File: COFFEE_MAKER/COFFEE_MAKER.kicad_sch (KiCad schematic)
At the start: 54 parts, among them J1 Conn_01x04, J2 Conn_01x06, J3 Conn_01x02_Pin, J4 Screw_Terminal_01x02, J5 USB_C_Receptacle_USB2.0_16P, J6 Conn_01x02_Pin, Q1 BC850, SW5 Reset, SW6 Boot, U3 AMS1117-3.3, U4 PCF8574, U5 MAX31855KASA, U6 AMS1117-5.0, U7 LD1117S33TR_SOT223, U8 ESP32-S2-SOLO

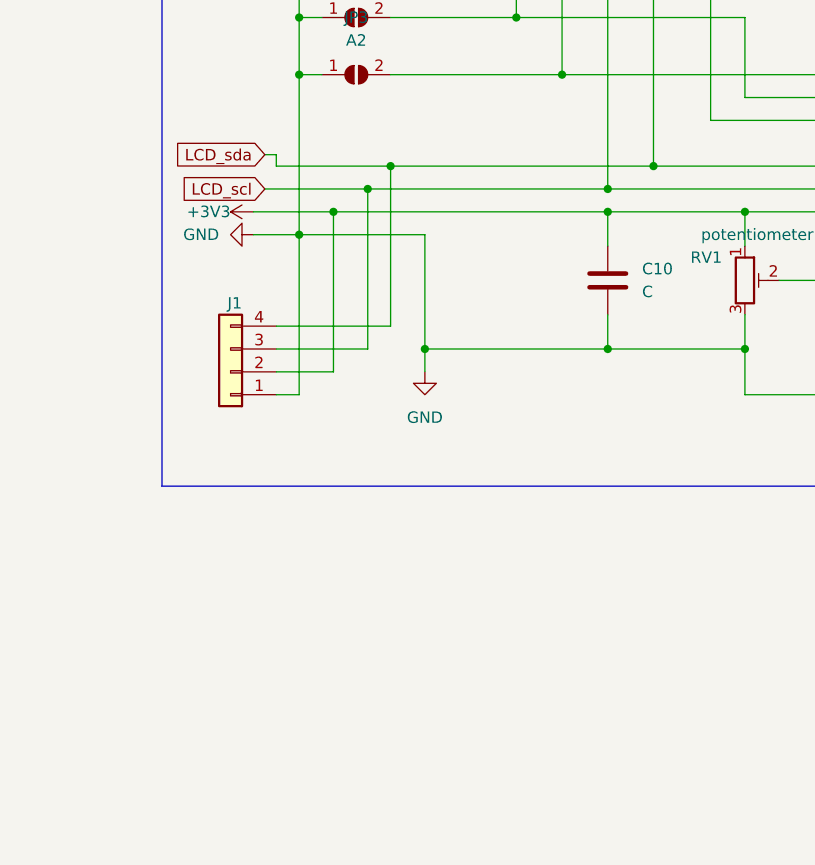
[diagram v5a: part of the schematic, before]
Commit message: added backup i2c pin, change lcd voltage to 5v
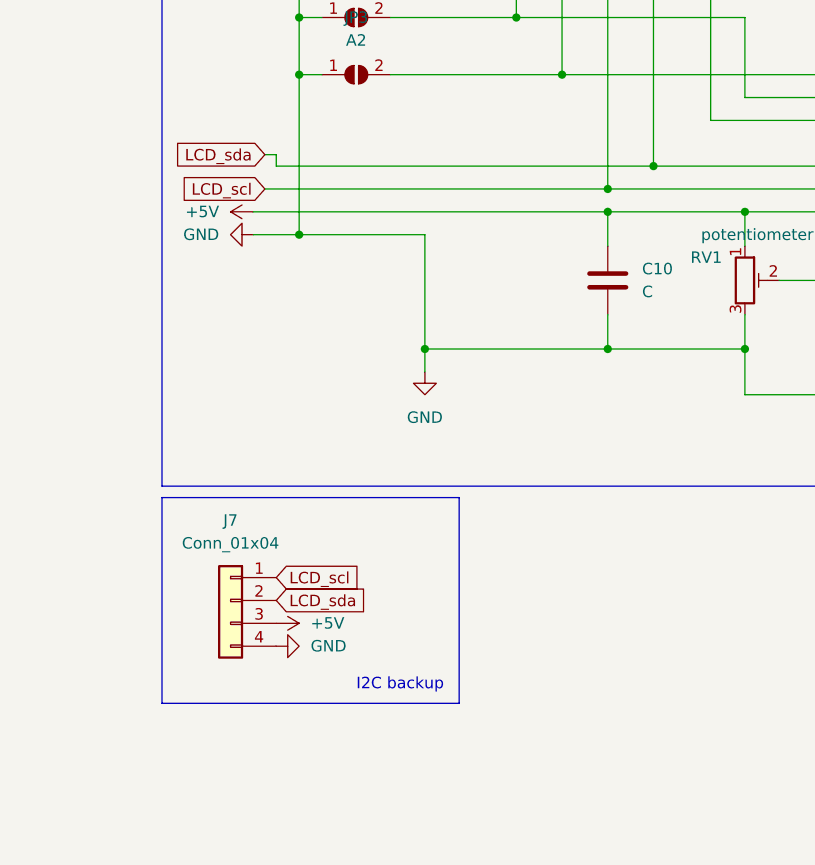
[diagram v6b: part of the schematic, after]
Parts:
- removed J1: Conn_01x04, symbol Connector_Generic:Conn_01x04
- added J7: Conn_01x04, symbol Connector_Generic:Conn_01x04
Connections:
- net +3V3: no longer C10.1, C16.1, C4.2, DS1.4 (VDD), F2.2, J5.A4 (VBUS), J5.A9 (VBUS), J5.B4 (VBUS), J5.B9 (VBUS), JP4.2 (B), R11.1, R12.1, R13.2, R14.1, R5.1, R6.1, R7.1, RV1.1, U4.8 (VSS), U7.3 (VI)
- net GND: now also J7.4 (Pin_4)
- net LCD_scl: now also J7.1 (Pin_1)
- net LCD_sda: now also J7.2 (Pin_2)
- new net +5V: C10.1, C16.1, C4.2, DS1.4 (VDD), F2.2, J5.A4 (VBUS), J5.A9 (VBUS), J5.B4 (VBUS), J5.B9 (VBUS), J7.3 (Pin_3), JP4.2 (B), R11.1, R12.1, R13.2, R14.1, R5.1, R6.1, R7.1, RV1.1, U4.8 (VSS), U7.3 (VI)
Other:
- note added: "I2C backup"
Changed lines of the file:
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@@
   (junction (at 207.01 124.46) (diameter 0) (color 0 0 0 0)
   )
-  (junction (at 38.1 57.15) (diameter 0) (color 0 0 0 0)
-  )
   (junction (at -229.87 106.68) (diameter 0) (color 0 0 0 0)
   )
@@
   (junction (at -29.21 60.96) (diameter 0) (color 0 0 0 0)
   )
-  (junction (at 35.56 59.69) (diameter 0) (color 0 0 0 0)
-  )
   (junction (at -165.1 35.56) (diameter 0) (color 0 0 0 0)
   )
@@
   )
   (junction (at 255.27 130.81) (diameter 0) (color 0 0 0 0)
-  )
-  (junction (at 31.75 62.23) (diameter 0) (color 0 0 0 0)
   )
   (junction (at -161.29 35.56) (diameter 0) (color 0 0 0 0)
@@
   (no_connect (at -58.42 60.96))
   (no_connect (at -149.86 58.42))
-  (wire (pts (xy 25.4 80.01) (xy 31.75 80.01))
-    (stroke (width 0) (type default))
-  )
   (wire (pts (xy 217.17 128.27) (xy 217.17 124.46))
     (stroke (width 0) (type default))
   )
-  (wire (pts (xy 35.56 59.69) (xy 62.23 59.69))
-    (stroke (width 0) (type default))
-  )
   (wire (pts (xy 77.47 62.23) (xy 90.17 62.23))
     (stroke (width 0) (type default))
@@
     (stroke (width 0) (type default))
   )
-  (wire (pts (xy 38.1 57.15) (xy 67.31 57.15))
-    (stroke (width 0) (type default))
-  )
   (wire (pts (xy -204.47 31.75) (xy -204.47 33.02))
     (stroke (width 0) (type default))
@@
     (stroke (width 0) (type default))
   )
-  (wire (pts (xy 25.4 77.47) (xy 35.56 77.47))
-    (stroke (width 0) (type default))
-  )
   (wire (pts (xy 165.1 69.85) (xy 132.08 69.85))
     (stroke (width 0) (type default))
@@
     (stroke (width 0) (type default))
   )
-  (wire (pts (xy 25.4 82.55) (xy 27.94 82.55))
-    (stroke (width 0) (type default))
-  )
   (wire (pts (xy 140.97 41.91) (xy 140.97 57.15))
     (stroke (width 0) (type default))
@@
     (stroke (width 0) (type default))
   )
-  (wire (pts (xy 27.94 82.55) (xy 27.94 64.77))
-    (stroke (width 0) (type default))
-  )
   (wire (pts (xy 137.16 77.47) (xy 119.38 77.47))
     (stroke (width 0) (type default))
@@
     (stroke (width 0) (type default))
   )
-  (wire (pts (xy 31.75 62.23) (xy 62.23 62.23))
-    (stroke (width 0) (type default))
-  )
   (wire (pts (xy -161.29 35.56) (xy -149.86 35.56))
     (stroke (width 0) (type default))
@@
     (stroke (width 0) (type default))
   )
-  (wire (pts (xy 24.13 59.69) (xy 35.56 59.69))
+  (wire (pts (xy 24.13 59.69) (xy 62.23 59.69))
     (stroke (width 0) (type default))
   )
@@
     (stroke (width 0) (type default))
   )
-  (wire (pts (xy 25.4 74.93) (xy 38.1 74.93))
-    (stroke (width 0) (type default))
-  )
   (wire (pts (xy 90.17 21.59) (xy 77.47 21.59))
     (stroke (width 0) (type default))
@@
     (stroke (width 0) (type default))
   )
-  (wire (pts (xy 22.86 62.23) (xy 31.75 62.23))
+  (wire (pts (xy 22.86 62.23) (xy 62.23 62.23))
     (stroke (width 0) (type default))
   )
@@
     (stroke (width 0) (type default))
   )
-  (wire (pts (xy 38.1 74.93) (xy 38.1 57.15))
-    (stroke (width 0) (type default))
-  )
   (wire (pts (xy 252.73 125.73) (xy 261.62 125.73))
     (stroke (width 0) (type default))
@@
     (stroke (width 0) (type default))
   )
-  (wire (pts (xy 35.56 77.47) (xy 35.56 59.69))
-    (stroke (width 0) (type default))
-  )
   (wire (pts (xy 241.3 130.81) (xy 245.11 130.81))
     (stroke (width 0) (type default))
@@
     (stroke (width 0) (type default))
   )
-  (wire (pts (xy 31.75 80.01) (xy 31.75 62.23))
-    (stroke (width 0) (type default))
-  )
   (wire (pts (xy -58.42 50.8) (xy -39.37 50.8))
     (stroke (width 0) (type default))
@@
     (stroke (width 0) (type default))
   )
-  (wire (pts (xy 25.4 57.15) (xy 38.1 57.15))
+  (wire (pts (xy 25.4 57.15) (xy 67.31 57.15))
     (stroke (width 0) (type default))
   )
@@
     (fill (type none))
   )
+  (rectangle (start 45.72 116.84) (end 12.7 93.98)
+    (stroke (width 0) (type default))
+    (fill (type none))
+  )
   (rectangle (start 124.46 114.3) (end 153.67 146.05)
     (stroke (width 0) (type default))
@@
   )
   (text "LCD I2C" (at 158.75 91.44 0)
+    (effects (font (size 1.27 1.27)) (justify left bottom))
+  )
+  (text "I2C backup\n" (at 34.29 115.57 0)
     (effects (font (size 1.27 1.27)) (justify left bottom))
   )
@@
     )
   )
+  (global_label "LCD_sda" (shape input) (at 25.4 105.41 0) (fields_autoplaced)
+    (effects (font (size 1.27 1.27)) (justify left))
+    (property "Intersheetrefs" "${INTERSHEET_REFS}" (at 36.247 105.41 0)
+      (effects (font (size 1.27 1.27)) (justify left) hide)
+    )
+  )
   (global_label "TC_cs" (shape input) (at -48.26 88.9 0) (fields_autoplaced)
     (effects (font (size 1.27 1.27)) (justify left))
@@
     )
   )
+  (global_label "LCD_scl" (shape input) (at 25.4 102.87 0) (fields_autoplaced)
+    (effects (font (size 1.27 1.27)) (justify left))
+    (property "Intersheetrefs" "${INTERSHEET_REFS}" (at 35.7028 102.87 0)
+      (effects (font (size 1.27 1.27)) (justify left) hide)
+    )
+  )
   (global_label "LCD_scl" (shape input) (at -48.26 74.93 0) (fields_autoplaced)
     (effects (font (size 1.27 1.27)) (justify left))
@@
         (path "/d1855ae5-bac9-4f6d-b11e-fad99d05f143"
           (reference "RV1") (unit 1)
+        )
+      )
+    )
+  )
+  (symbol (lib_id "power:+5V") (at 25.4 107.95 270) (unit 1)
+    (in_bom yes) (on_board yes) (dnp no) (fields_autoplaced)
+    (property "Reference" "#PWR08" (at 21.59 107.95 0)
+      (effects (font (size 1.27 1.27)) hide)
+    )
+    (property "Value" "+5V" (at 29.21 107.95 90)
+      (effects (font (size 1.27 1.27)) (justify left))
+    )
+    (property "Footprint" "" (at 25.4 107.95 0)
+      (effects (font (size 1.27 1.27)) hide)
+    )
+    (property "Datasheet" "" (at 25.4 107.95 0)
+      (effects (font (size 1.27 1.27)) hide)
+    )
+    (pin "1")
+    (instances
+      (project "COFFEE_MAKER"
+        (path "/d1855ae5-bac9-4f6d-b11e-fad99d05f143"
+          (reference "#PWR08") (unit 1)
         )
       )
@@
     )
   )
-  (symbol (lib_id "power:+3V3") (at 22.86 62.23 90) (unit 1)
-    (in_bom yes) (on_board yes) (dnp no)
-    (property "Reference" "#PWR02" (at 26.67 62.23 0)
-      (effects (font (size 1.27 1.27)) hide)
-    )
-    (property "Value" "+3V3" (at 20.32 62.23 90)
-      (effects (font (size 1.27 1.27)) (justify left))
-    )
-    (property "Footprint" "" (at 22.86 62.23 0)
-      (effects (font (size 1.27 1.27)) hide)
-    )
-    (property "Datasheet" "" (at 22.86 62.23 0)
-      (effects (font (size 1.27 1.27)) hide)
-    )
-    (pin "1")
-    (instances
-      (project "COFFEE_MAKER"
-        (path "/d1855ae5-bac9-4f6d-b11e-fad99d05f143"
-          (reference "#PWR02") (unit 1)
+  (symbol (lib_id "power:GND") (at 25.4 110.49 90) (unit 1)
+    (in_bom yes) (on_board yes) (dnp no) (fields_autoplaced)
+    (property "Reference" "#PWR012" (at 31.75 110.49 0)
+      (effects (font (size 1.27 1.27)) hide)
+    )
+    (property "Value" "GND" (at 29.21 110.49 90)
+      (effects (font (size 1.27 1.27)) (justify right))
+    )
+    (property "Footprint" "" (at 25.4 110.49 0)
+      (effects (font (size 1.27 1.27)) hide)
+    )
+    (property "Datasheet" "" (at 25.4 110.49 0)
+      (effects (font (size 1.27 1.27)) hide)
+    )
+    (pin "1")
+    (instances
+      (project "COFFEE_MAKER"
+        (path "/d1855ae5-bac9-4f6d-b11e-fad99d05f143"
+          (reference "#PWR012") (unit 1)
         )
       )
@@
     )
   )
-  (symbol (lib_id "Connector_Generic:Conn_01x04") (at 20.32 80.01 180) (unit 1)
-    (in_bom yes) (on_board yes) (dnp no)
-    (property "Reference" "J1" (at 21.59 72.39 0)
-      (effects (font (size 1.27 1.27)) (justify left))
-    )
-    (property "Value" "Conn_01x04" (at 26.67 69.85 0)
-      (effects (font (size 1.27 1.27)) (justify left) hide)
-    )
-    (property "Footprint" "" (at 20.32 80.01 0)
-      (effects (font (size 1.27 1.27)) hide)
-    )
-    (property "Datasheet" "~" (at 20.32 80.01 0)
-      (effects (font (size 1.27 1.27)) hide)
-    )
-    (pin "2")
-    (pin "1")
-    (pin "3")
-    (pin "4")
-    (instances
-      (project "COFFEE_MAKER"
-        (path "/d1855ae5-bac9-4f6d-b11e-fad99d05f143"
-          (reference "J1") (unit 1)
-        )
-      )
-    )
-  )
   (symbol (lib_id "power:+3V3") (at 227.33 120.65 0) (unit 1)
     (in_bom yes) (on_board yes) (dnp no) (fields_autoplaced)
@@
     )
   )
+  (symbol (lib_id "power:+5V") (at 22.86 62.23 90) (unit 1)
+    (in_bom yes) (on_board yes) (dnp no) (fields_autoplaced)
+    (property "Reference" "#PWR02" (at 26.67 62.23 0)
+      (effects (font (size 1.27 1.27)) hide)
+    )
+    (property "Value" "+5V" (at 19.05 62.23 90)
+      (effects (font (size 1.27 1.27)) (justify left))
+    )
+    (property "Footprint" "" (at 22.86 62.23 0)
+      (effects (font (size 1.27 1.27)) hide)
+    )
+    (property "Datasheet" "" (at 22.86 62.23 0)
+      (effects (font (size 1.27 1.27)) hide)
+    )
+    (pin "1")
+    (instances
+      (project "COFFEE_MAKER"
+        (path "/d1855ae5-bac9-4f6d-b11e-fad99d05f143"
+          (reference "#PWR02") (unit 1)
+        )
+      )
+    )
+  )
   (symbol (lib_id "power:GND") (at 227.33 140.97 0) (unit 1)
     (in_bom yes) (on_board yes) (dnp no) (fields_autoplaced)
@@
         )
       )
+    )
+  )
+  (symbol (lib_id "Connector_Generic:Conn_01x04") (at 20.32 105.41 0) (mirror y) (unit 1)
+    (in_bom yes) (on_board yes) (dnp no) (fields_autoplaced)
+    (property "Reference" "J7" (at 20.32 96.52 0)
+      (effects (font (size 1.27 1.27)))
+    )
+    (property "Value" "Conn_01x04" (at 20.32 99.06 0)
+      (effects (font (size 1.27 1.27)))
+    )
+    (property "Footprint" "" (at 20.32 105.41 0)
+      (effects (font (size 1.27 1.27)) hide)
+    )
+    (property "Datasheet" "~" (at 20.32 105.41 0)
+      (effects (font (size 1.27 1.27)) hide)
+    )
+    (pin "4")
+    (pin "2")
+    (pin "3")
+    (pin "1")
+    (instances
+      (project "COFFEE_MAKER"
+        (path "/d1855ae5-bac9-4f6d-b11e-fad99d05f143"
+          (reference "J7") (unit 1)
+        )
+      )

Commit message: added connector for pin
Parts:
- removed J3, J6: Conn_01x02_Pin, Connector_PinHeader_2.54mm:PinHeader_1x02_P2.54mm_Vertical, symbol Connector:Conn_01x02_Pin
- added J1, J3: Conn_01x03_Pin, Connector_PinHeader_2.54mm:PinHeader_1x03_P2.54mm_Horizontal, symbol Connector:Conn_01x03_Pin
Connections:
- net +3.3V: now also J1.1 (Pin_1), J3.1 (Pin_1)
- net GND: now also J1.3 (Pin_3), J3.3 (Pin_3)
- net RELAY_COIL: now reaches U8.38 (GPIO2/TOUCH2/ADC1_CH1)
- net RELAY_COIL: now also J1.2 (Pin_2)
- net RELAY_FAN: now reaches U8.39 (GPIO1/TOUCH1/ADC1_CH0)
- net RELAY_FAN: now also J3.2 (Pin_2)
- no-connect marks 36 -> 34

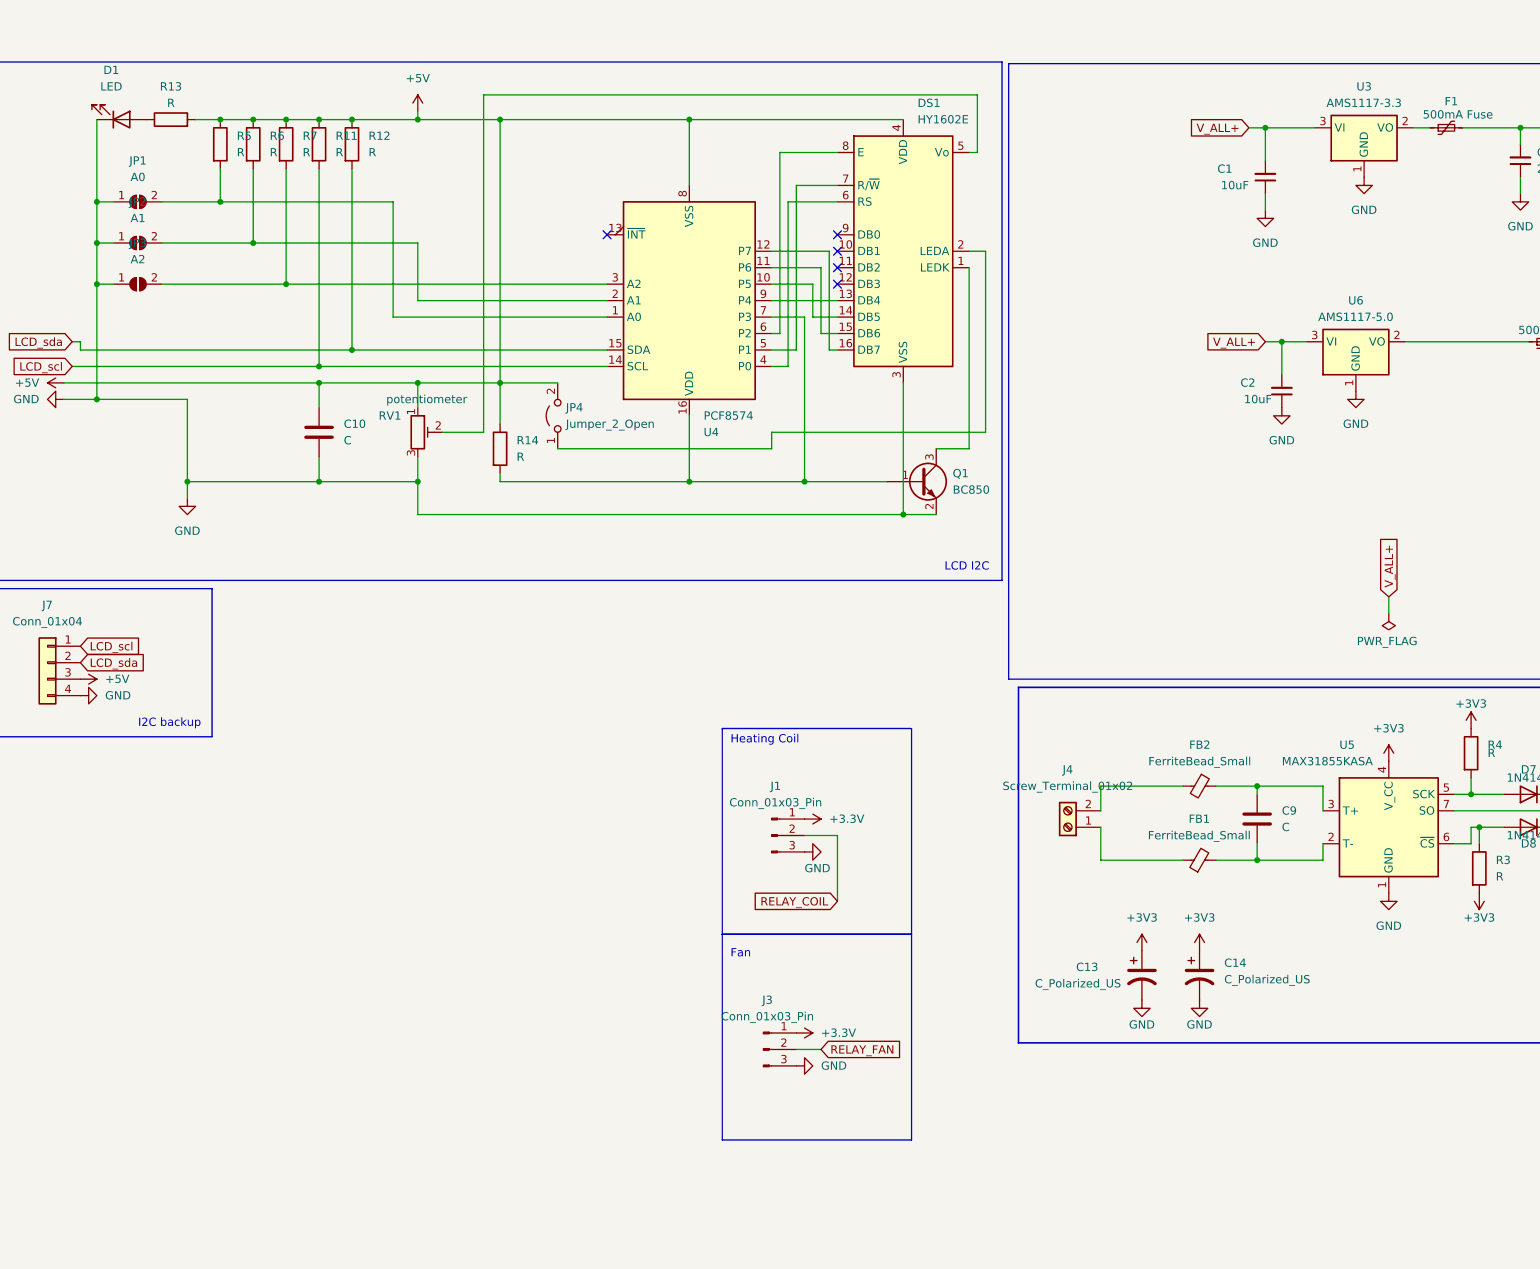
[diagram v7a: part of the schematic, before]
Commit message: schematic update
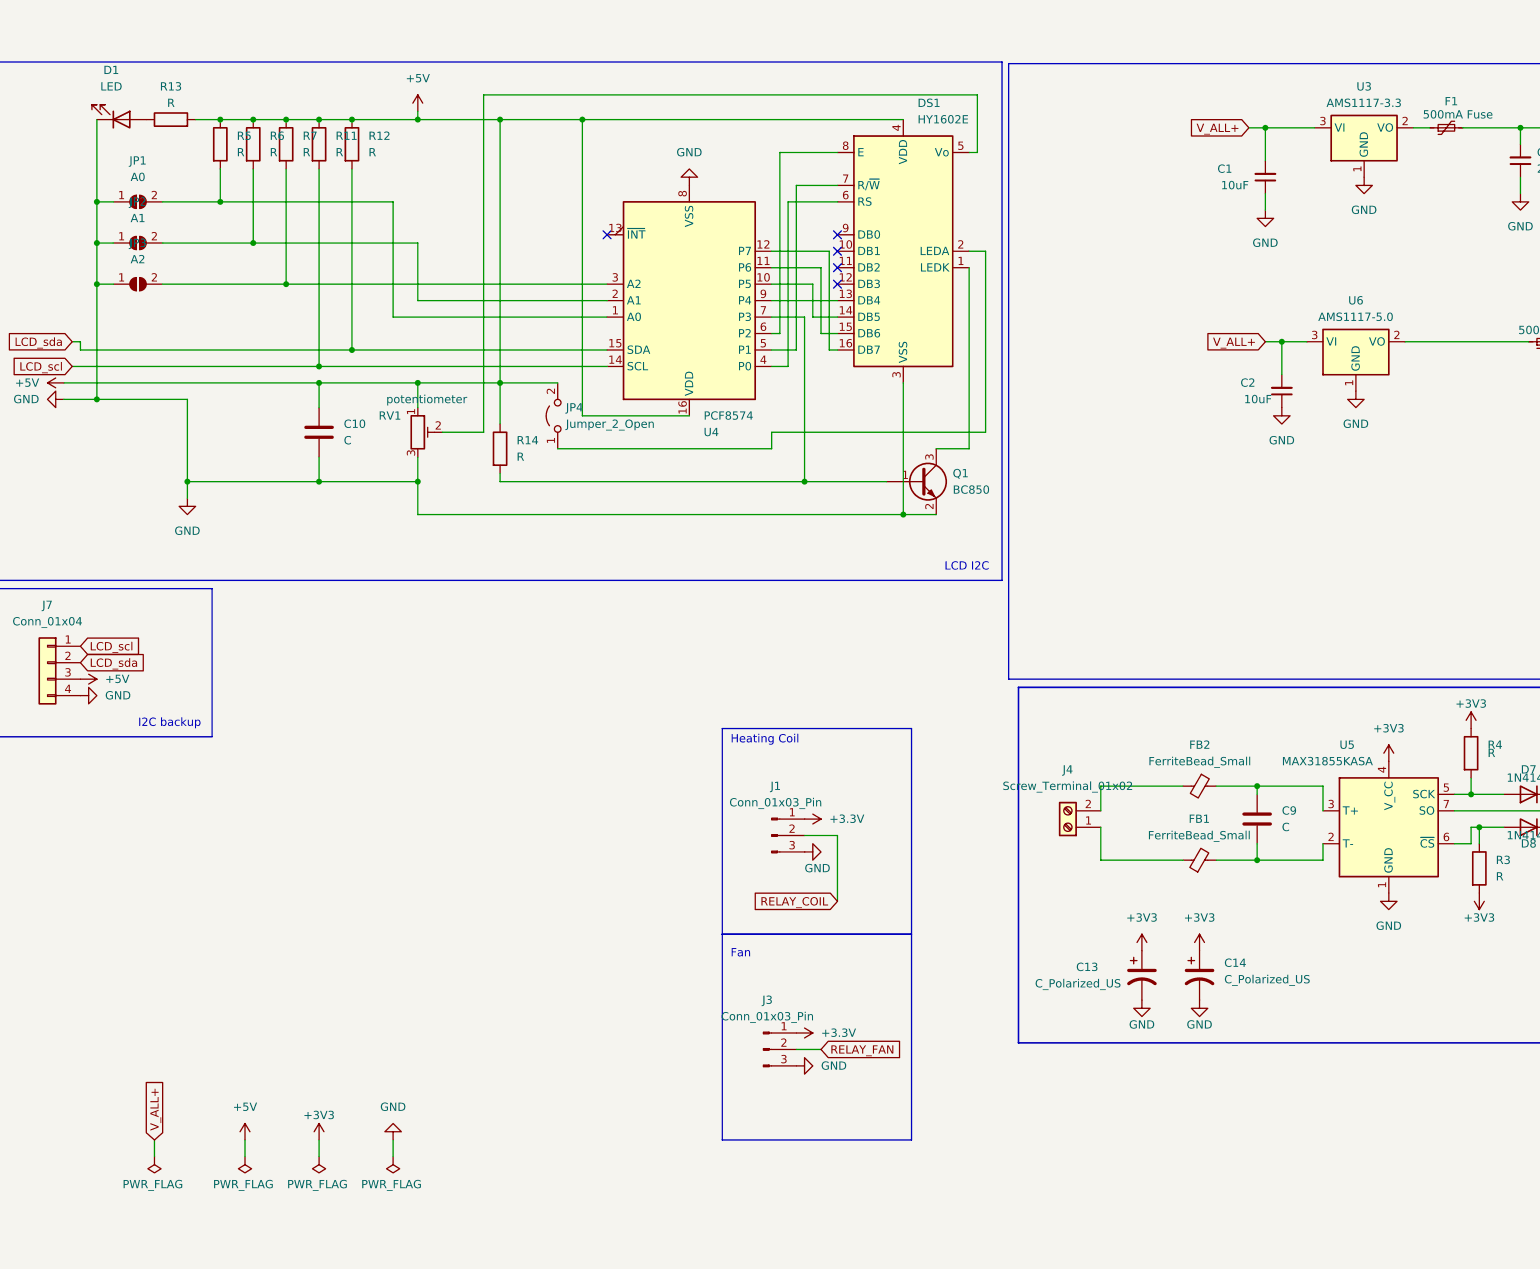
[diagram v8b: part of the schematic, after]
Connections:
- net +5V: now also U4.16 (VDD); no longer U4.8 (VSS)
- net GND: now also U4.8 (VSS)
- net at Q1.1 (B), R14.2, U4.7 (P3): no longer U4.16 (VDD)
